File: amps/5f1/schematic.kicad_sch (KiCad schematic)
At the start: 26 parts, among them T2 SE 5k:8

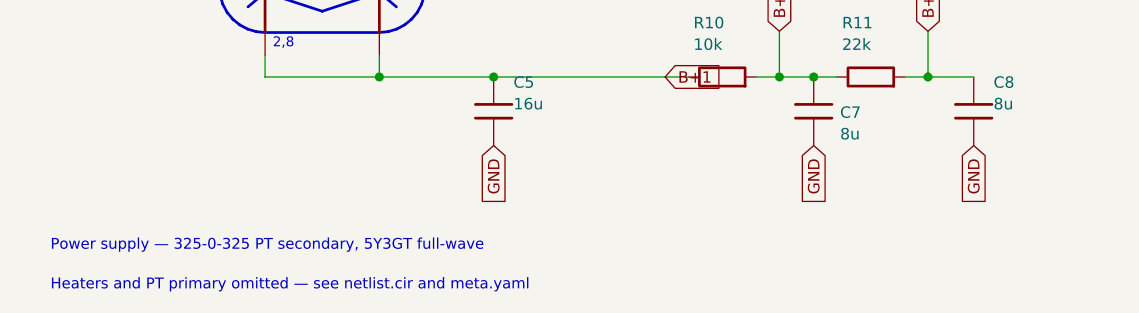
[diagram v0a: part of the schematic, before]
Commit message: Fix: 5F1 sheet footnote — the fix the previous commit claimed had not applied
6e05cd3 said "the sheet's footnote no longer names repo files". It did: the
replacement in draw_5f1.py matched nothing and the commit went out on the
strength of the message rather than the diff. This commit makes the change —
"see netlist.cir and meta.yaml" becomes "see the board drawing and the sources
cited on this page" — and the regenerated sheet is checked for the strings.

Co-Authored-By: Claude Fable 5.1 <noreply@anthropic.com>
Claude-Session: https://claude.ai/code/session_01KBMfdh37HmCL2iWcBiL5J1
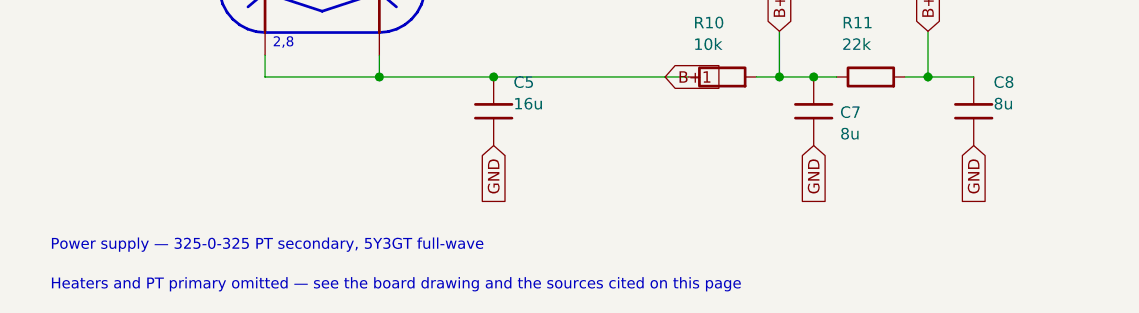
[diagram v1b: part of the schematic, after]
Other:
- note added: "Heaters and PT primary omitted — see the board drawing and the sources cited on this page"
- note removed: "Heaters and PT primary omitted — see netlist.cir and meta.yaml"
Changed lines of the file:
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@@
   (text "Power supply — 325-0-325 PT secondary, 5Y3GT full-wave" (at 12.7 117.076 0)
     (effects (font (size 1.2 1.2)) (justify left)))
-  (text "Heaters and PT primary omitted — see netlist.cir and meta.yaml" (at 12.7 121.476 0)
+  (text "Heaters and PT primary omitted — see the board drawing and the sources cited on this page" (at 12.7 121.476 0)
     (effects (font (size 1.2 1.2)) (justify left)))
   (sheet_instances (path "/" (page "1")))

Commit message: Fix: draw the 1 MΩ input grid leak on the jack-1 tip node, not the grid, on eight tweed/Champ sheets
Every tweed and Champ factory sheet hangs the 1 MΩ from the jack-1 tip
node (the node the jack-2 shorting contact also lands on) to ground, and
runs the 68 K stoppers from the jack tips to the grid. These eight sheets
drew the 1 MΩ on the GRID side of the stopper — one copy-pasted idiom in
four scripts and its cousins in four more; there is no shared helper, so
each script is fixed where it draws the block. The stopper is declared
DC-transparent (layout net_map.series_bridge), so the netlist sees one node
either way and verify_schematic_nets stays 40 clean; the sheet-vs-board
gate, which compares the drawings to each other, drops all twelve
MISPLACED findings (RG1/RG2 on 5e4a, 5e5a, 5f4, 5f6; R3 on 5f2a, aa764,
aa764-vibro; R1 on 5f1). 5f10's jack chain is a separate task.

Crops read: 5e4a-RG1-RG2-input.png, 5e5a-RG1-RG2-input.png,
5f4-RG1-input.png, 5f6-RG1-RG2-input.png, 5f2a-R3-input.png,
5f1-R1-input.png, aa764-R3-input.png, aa764-vibro-R3-input.png — each
prints "1 MEG." from the jack-1 tip to ground with the 68K pair to the grid.

Geometry: the four two-channel sheets hang the leak from the stopper's
jack-side pin; 5f1 drops it from the INPUT line; 5f2a and the two Champs
stand it upward off the jack-1 line because the jack-2 line runs 8–12 mm
below. Previews read cleanly. The circuit stories already say the leaks
mount at the jacks, so no prose changed.

Gates: check_schematics 40/0 (0 isolated), verify_schematic_nets 40
clean, validate/value-consistency/era-values clean, regenerate-all leaves
every other sheet byte-identical. verify_sheet_vs_board misplaced 98 -> 86.

Co-Authored-By: Claude Fable 5.1 <noreply@anthropic.com>
Claude-Session: https://claude.ai/code/session_01KBMfdh37HmCL2iWcBiL5J1
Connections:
- net INPUT: now also R1.1
- net at R3.2, V1A.2 (G): no longer R1.1
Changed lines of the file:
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@@
   (global_label "INPUT" (shape input) (at 18.7452 38.278 180)
     (effects (font (size 1.27 1.27)) (justify right)))
-  (wire (pts (xy 18.7452 38.278) (xy 27.6552 38.278))
+  (wire (pts (xy 18.7452 38.278) (xy 23.2452 38.278))
+    (stroke (width 0) (type default)))
+  (wire (pts (xy 23.2452 38.278) (xy 27.6552 38.278))
     (stroke (width 0) (type default)))
   (symbol (lib_id "cx:R") (at 31.4652 38.278 90) (unit 1)
@@
     (property "Reference" "V1A" (at 52.7052 31.878 0) (effects (font (size 1.27 1.27)) (justify left)))
     (property "Value" "12AX7" (at 52.7052 34.278 0) (effects (font (size 1.27 1.27)) (justify left))))
-  (junction (at 39.0852 38.278) (diameter 1) (color 0 0 0 0))
-  (symbol (lib_id "cx:R") (at 39.0852 48.768 0) (unit 1)
+  (junction (at 23.2452 38.278) (diameter 1) (color 0 0 0 0))
+  (wire (pts (xy 23.2452 38.278) (xy 23.2452 44.958))
+    (stroke (width 0) (type default)))
+  (symbol (lib_id "cx:R") (at 23.2452 48.768 0) (unit 1)
     (in_bom yes) (on_board yes)
-    (property "Reference" "R1" (at 41.2852 45.568 0) (effects (font (size 1.27 1.27)) (justify left)))
-    (property "Value" "1M" (at 41.2852 47.968 0) (effects (font (size 1.27 1.27)) (justify left))))
-  (wire (pts (xy 39.0852 38.278) (xy 39.0852 44.958))
-    (stroke (width 0) (type default)))
-  (global_label "GND" (shape input) (at 39.0852 52.578 270)
+    (property "Reference" "R1" (at 25.4452 45.568 0) (effects (font (size 1.27 1.27)) (justify left)))
+    (property "Value" "1M" (at 25.4452 47.968 0) (effects (font (size 1.27 1.27)) (justify left))))
+  (global_label "GND" (shape input) (at 23.2452 52.578 270)
     (effects (font (size 1.27 1.27)) (justify right)))
   (wire (pts (xy 46.7052 45.898) (xy 46.7052 50.038))

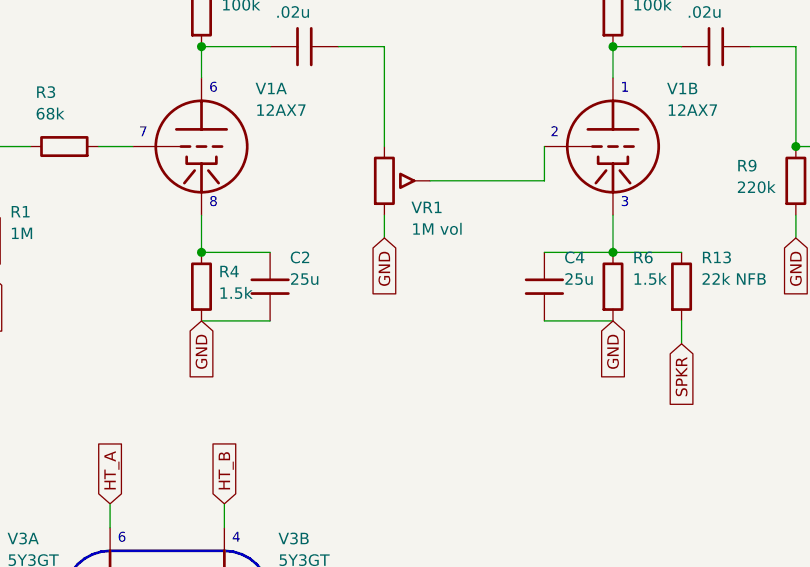
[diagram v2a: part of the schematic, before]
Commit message: Fix: the 5F1 sheet drew two cathode bypass capacitors its drawing does not have
K-EE (1306x994; every copy in circulation, Schematic Heaven's and
EL34World's, is this image) draws both 12AX7 cathodes as a bare 1500 to
ground: V1A's plain, V1B's with the 22K feedback from the speaker returning
to it. The one bypass on the sheet is the 25-25 across the 6V6's 470.

This sheet drew a 25 uF across each 1500 (C2, C4), the parts list carried
them, and the circuit story called V1A's cathode "bypassed". The netlist,
which models cathode-bypass capacitors wherever both leads are on modelled
nodes, never had them, so the corpus disagreed with itself; the
sheet-vs-board survey had already listed C2 and C4 as the only two 5F1
parts the board does not place. Removed from the sheet and the parts list
(the sequential designators keep the gap rather than renumbering the
netlist and the board); the story now says both 12AX7 cathodes are
unbypassed on the drawing. No DC figure moves. Found by the declaration
pass reading the board against K-EE; confirmed here on the schematic page.

Gates: check_schematics (connectivity 0 isolated pins), verify_schematic_nets
40 clean with the 5F1 claimed, tone gate, validate 41/0,
check_value_consistency --strict 0, test_era_values, verify_amps,
verify_sheet_vs_board drift clean after --export (the 5F1 now clean);
regenerating every sheet changes only this one.

Co-Authored-By: Claude Opus 5 (1M context) <noreply@anthropic.com>
Claude-Session: https://claude.ai/code/session_01KBMfdh37HmCL2iWcBiL5J1
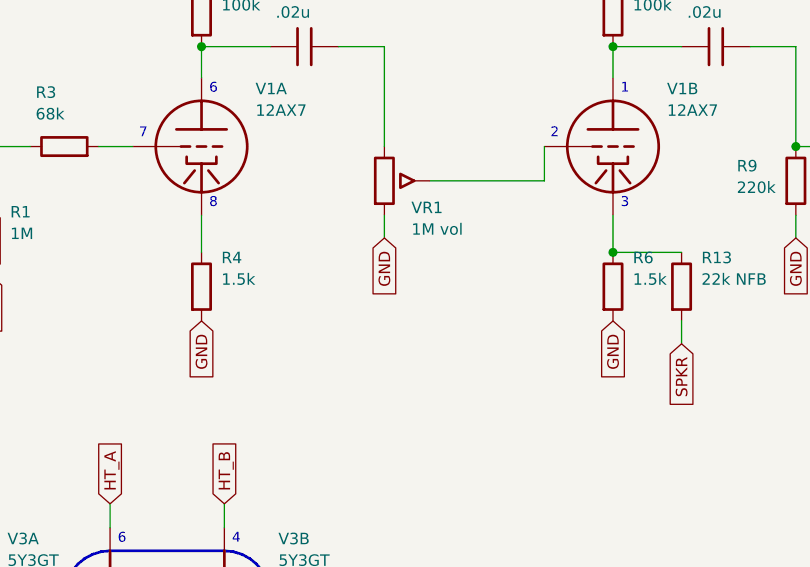
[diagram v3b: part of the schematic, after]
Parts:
- removed C1: .02u, symbol cx:C
- removed C2, C4: 25u, symbol cx:C
- removed T2: SE 5k:8, symbol cx:OT_SE
- added R5: 100k, symbol cx:R
- added V2: 6V6GT, symbol cx:PENTODE
- C1: renamed from R5; value 100k -> .02u; symbol cx:R -> cx:C
- R8: renamed from V2; value 6V6GT -> 470; symbol cx:PENTODE -> cx:R
- T2: renamed from R8; value 470 -> SE 5k:8; symbol cx:R -> cx:OT_SE
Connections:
- net B+1: now also T2.2 (PRI_B)
- net B+2: now also V2.3 (G2); no longer R8.3 (G2)
- net B+3: now also R5.1; no longer C1.1
- net GND: now also R8.2, T2.4 (SEC_C); no longer T2.2
- net SPKR: now also T2.3 (SEC_H)
- net at VR1.1: now also C1.2
- net at V1A.1 (P): now also C1.1, R5.2; no longer C1.2
- net at C3.2, R9.1: now also V2.2 (G1); no longer R8.2 (G1)
- net at R8.1: now also C6.1, V2.4 (K)
- new net: T2.1 (PRI_P), V2.1 (P)
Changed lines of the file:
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@@
   (wire (pts (xy 46.7052 45.898) (xy 46.7052 50.038))
     (stroke (width 0) (type default)))
-  (junction (at 46.7052 50.038) (diameter 1) (color 0 0 0 0))
   (symbol (lib_id "cx:R") (at 46.7052 53.848 0) (unit 1)
     (in_bom yes) (on_board yes)
-    (property "Reference" "R4" (at 48.6212 52.208 0) (effects (font (size 1.27 1.27)) (justify left)))
-    (property "Value" "1.5k" (at 48.6212 54.608 0) (effects (font (size 1.27 1.27)) (justify left))))
-  (wire (pts (xy 46.7052 50.038) (xy 54.3252 50.038))
-    (stroke (width 0) (type default)))
-  (symbol (lib_id "cx:C") (at 54.3252 53.848 0) (unit 1)
-    (in_bom yes) (on_board yes)
-    (property "Reference" "C2" (at 56.5252 50.648 0) (effects (font (size 1.27 1.27)) (justify left)))
-    (property "Value" "25u" (at 56.5252 53.048 0) (effects (font (size 1.27 1.27)) (justify left))))
-  (wire (pts (xy 46.7052 57.658) (xy 54.3252 57.658))
-    (stroke (width 0) (type default)))
+    (property "Reference" "R4" (at 48.9052 50.648 0) (effects (font (size 1.27 1.27)) (justify left)))
+    (property "Value" "1.5k" (at 48.9052 53.048 0) (effects (font (size 1.27 1.27)) (justify left))))
   (global_label "GND" (shape input) (at 46.7052 57.658 270)
     (effects (font (size 1.27 1.27)) (justify right)))
@@
     (property "Reference" "R6" (at 94.6252 50.648 0) (effects (font (size 1.27 1.27)) (justify left)))
     (property "Value" "1.5k" (at 94.6252 53.048 0) (effects (font (size 1.27 1.27)) (justify left))))
-  (wire (pts (xy 92.4252 50.038) (xy 84.8052 50.038))
-    (stroke (width 0) (type default)))
-  (symbol (lib_id "cx:C") (at 84.8052 53.848 0) (unit 1)
-    (in_bom yes) (on_board yes)
-    (property "Reference" "C4" (at 87.0052 50.648 0) (effects (font (size 1.27 1.27)) (justify left)))
-    (property "Value" "25u" (at 87.0052 53.048 0) (effects (font (size 1.27 1.27)) (justify left))))
-  (wire (pts (xy 84.8052 57.658) (xy 92.4252 57.658))
-    (stroke (width 0) (type default)))
   (global_label "GND" (shape input) (at 92.4252 57.658 270)
     (effects (font (size 1.27 1.27)) (justify right)))

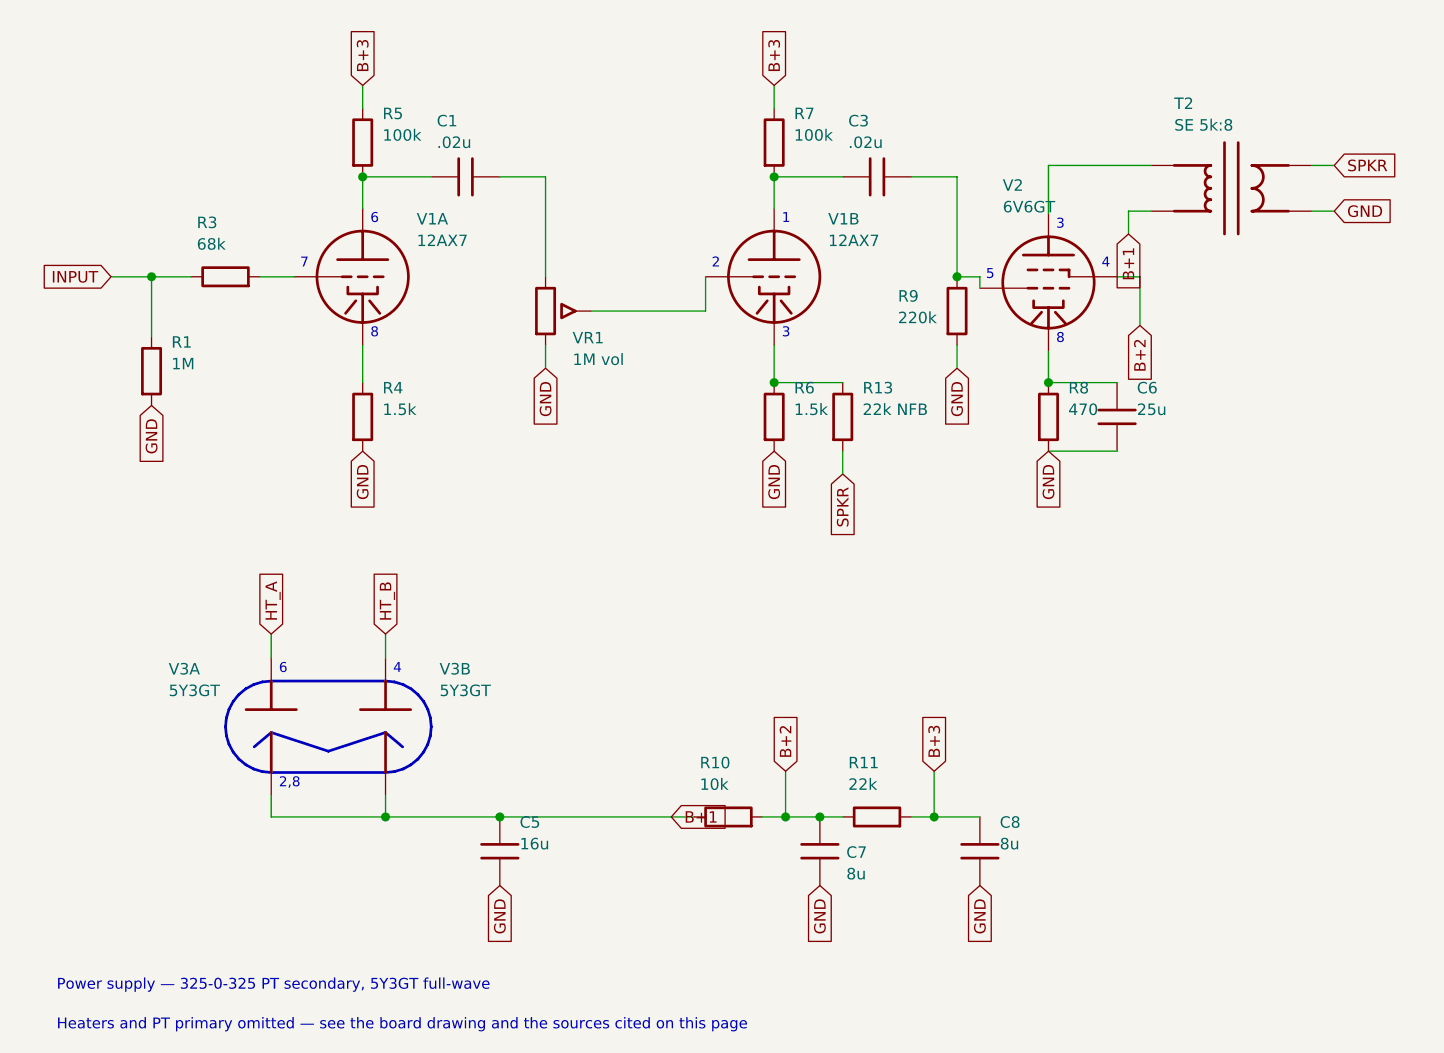
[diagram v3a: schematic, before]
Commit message: 5F1: each input jack has its own 68 kΩ stopper (V1 audit)
K-EE draws two 68 Ks, one from each jack's tip to the V1A grid, on both
pages (cited copy, the only one found: schematic page 1306x994 crop
0,290,300,260; layout page 1147x988 crop 800,150,300,300). The corpus
carried one shared 68 K: the BOM had no second stopper, the sheet drew a
single INPUT, and the board ran both jacks into R3, a simplification the
layout caption stated outright. R2 (68 k) is added to the BOM, the sheet
(INPUT 2) and the board (J2 -> R2 -> V1A grid, declared a series_bridge).
The 1 M leak stays at jack 1's tip; R3 and R1 roles say so. The board
widens by two columns to seat R2 at the input end. No DC node moves.

Co-Authored-By: Claude Opus 5.5 <noreply@anthropic.com>
Claude-Session: https://claude.ai/code/session_01KBMfdh37HmCL2iWcBiL5J1
Signed-off-by: AnalogMaker <theanalogmaker@gmail.com>
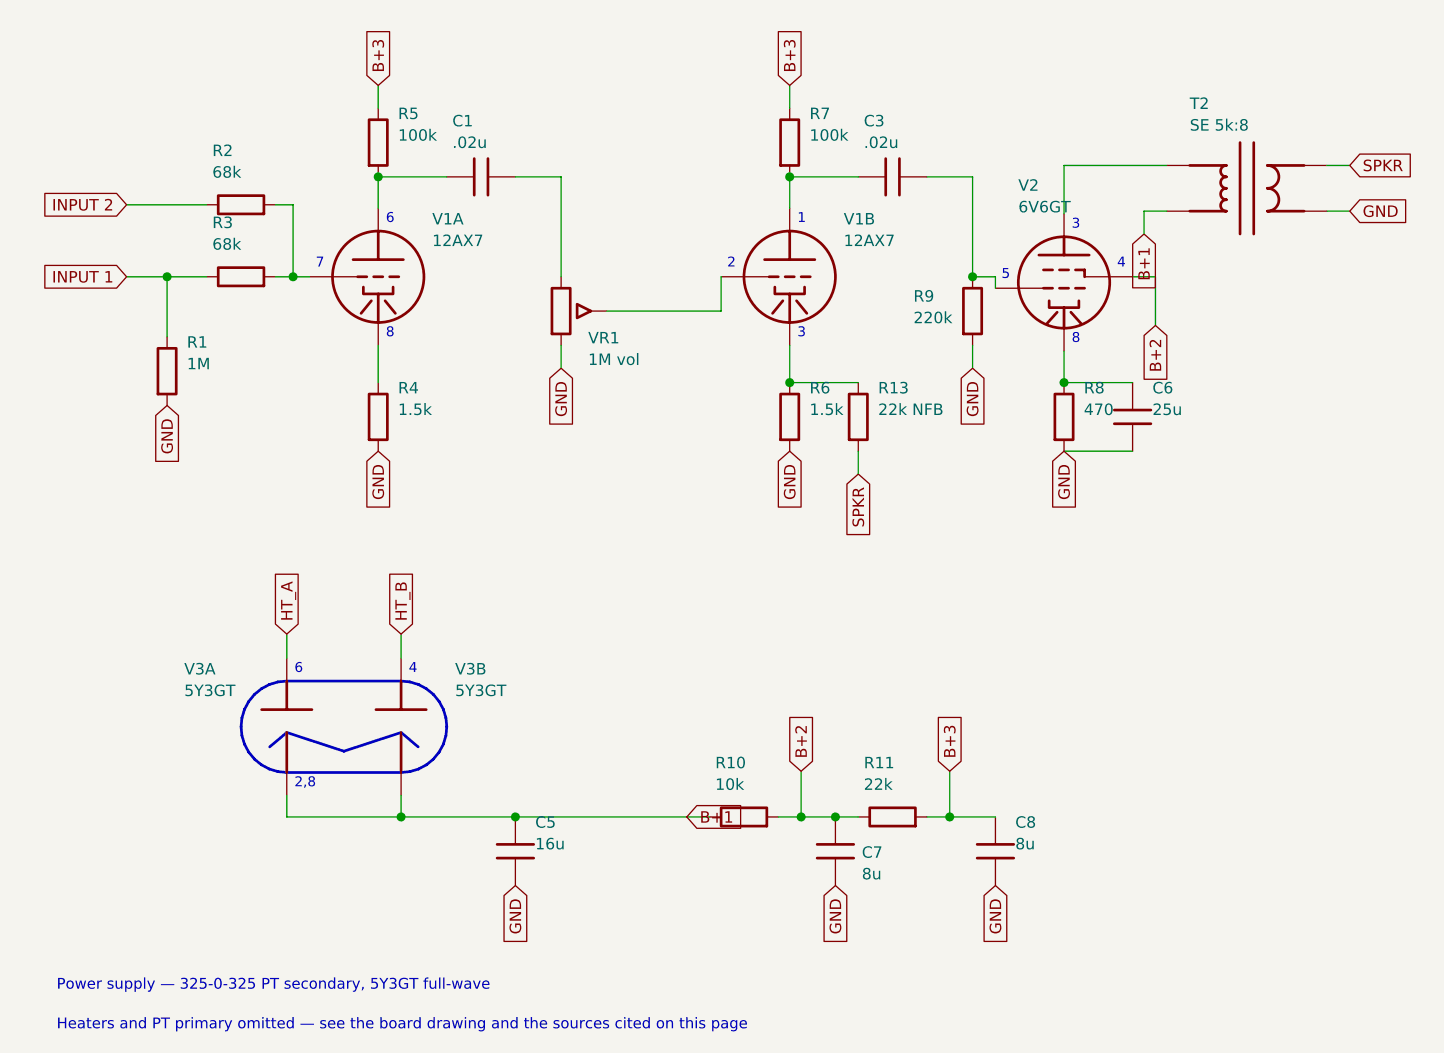
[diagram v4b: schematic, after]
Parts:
- removed V2: 6V6GT, symbol cx:PENTODE
- added T2: SE 5k:8, symbol cx:OT_SE
- added VR1: 1M vol, symbol cx:POT
- R1: renamed from R5; value 100k -> 1M
- R2: renamed from R1; value 1M -> 68k
- R5: renamed from VR1; value 1M vol -> 100k; symbol cx:POT -> cx:R
- R8: renamed from T2; value SE 5k:8 -> 470; symbol cx:OT_SE -> cx:R
- V2: renamed from R8; value 470 -> 6V6GT; symbol cx:R -> cx:PENTODE
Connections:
- net B+1: now also T2.2 (PRI_B); no longer R8.2 (PRI_B)
- net B+2: now also V2.3 (G2)
- net B+3: now also R5.1; no longer R1.1
- net GND: now also R1.2, R8.2, T2.4 (SEC_C), VR1.3; no longer R2.2, R5.3, R8.4 (SEC_C), V2.2
- net SPKR: now also T2.3 (SEC_H); no longer R8.3 (SEC_H)
- net at C1.1, V1A.1 (P): now also R5.2; no longer R1.2
- net at C1.2: now also VR1.1; no longer R5.1
- net at C3.2, R9.1: now also V2.2 (G1)
- net at C6.1: now also R8.1, V2.4 (K); no longer V2.1
- net at V1B.2 (G): now also VR1.2 (W); no longer R5.2 (W)
- net at R3.2, V1A.2 (G): now also R2.2
- net INPUT renamed INPUT 1
- net INPUT 1: now also R1.1; no longer R2.1
- new net: T2.1 (PRI_P), V2.1 (P)
- new net INPUT 2: R2.1
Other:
- moved on the sheet: R1, R2, R3
